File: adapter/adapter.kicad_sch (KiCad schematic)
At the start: 13 parts, among them J1 Serial, J10 Ribbon, J3 Battery charge, J4 RGB, J9 Ribbon, SW1 SW_SPST, SW3 SW_SPDT, U1 Dual MCU: RP2040 + nice!nano

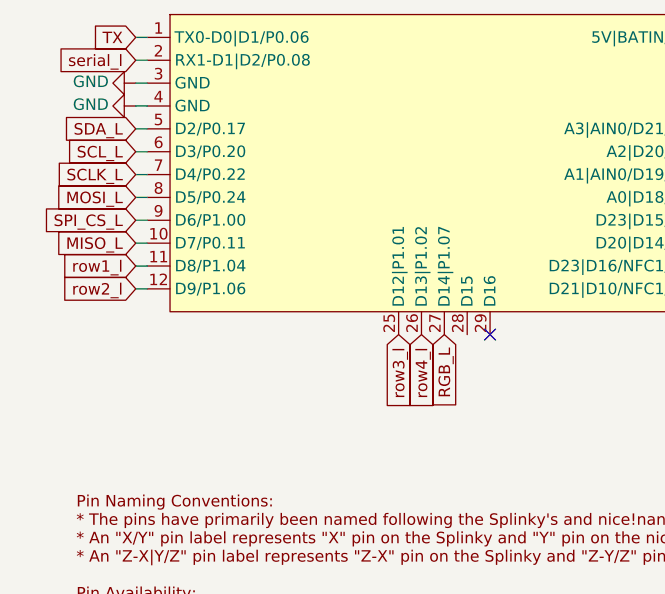
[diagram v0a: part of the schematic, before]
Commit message: sch: properly assign spi pins
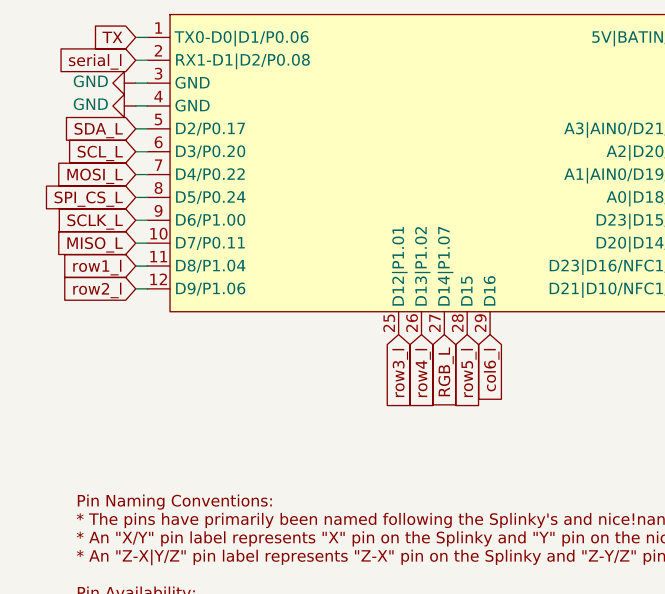
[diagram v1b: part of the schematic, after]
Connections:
- net MOSI_L: now also U1.7 (D4/P0.22); no longer U1.8 (D5/P0.24)
- net SCLK_L: now also U1.9 (D6/P1.00); no longer U1.7 (D4/P0.22)
- net SPI_CS_L: now also U1.8 (D5/P0.24); no longer U1.9 (D6/P1.00)
- net col6_l: now also U1.29 (D16)
- net row5_l: now also U1.28 (D15)
- no-connect marks 3 -> 2

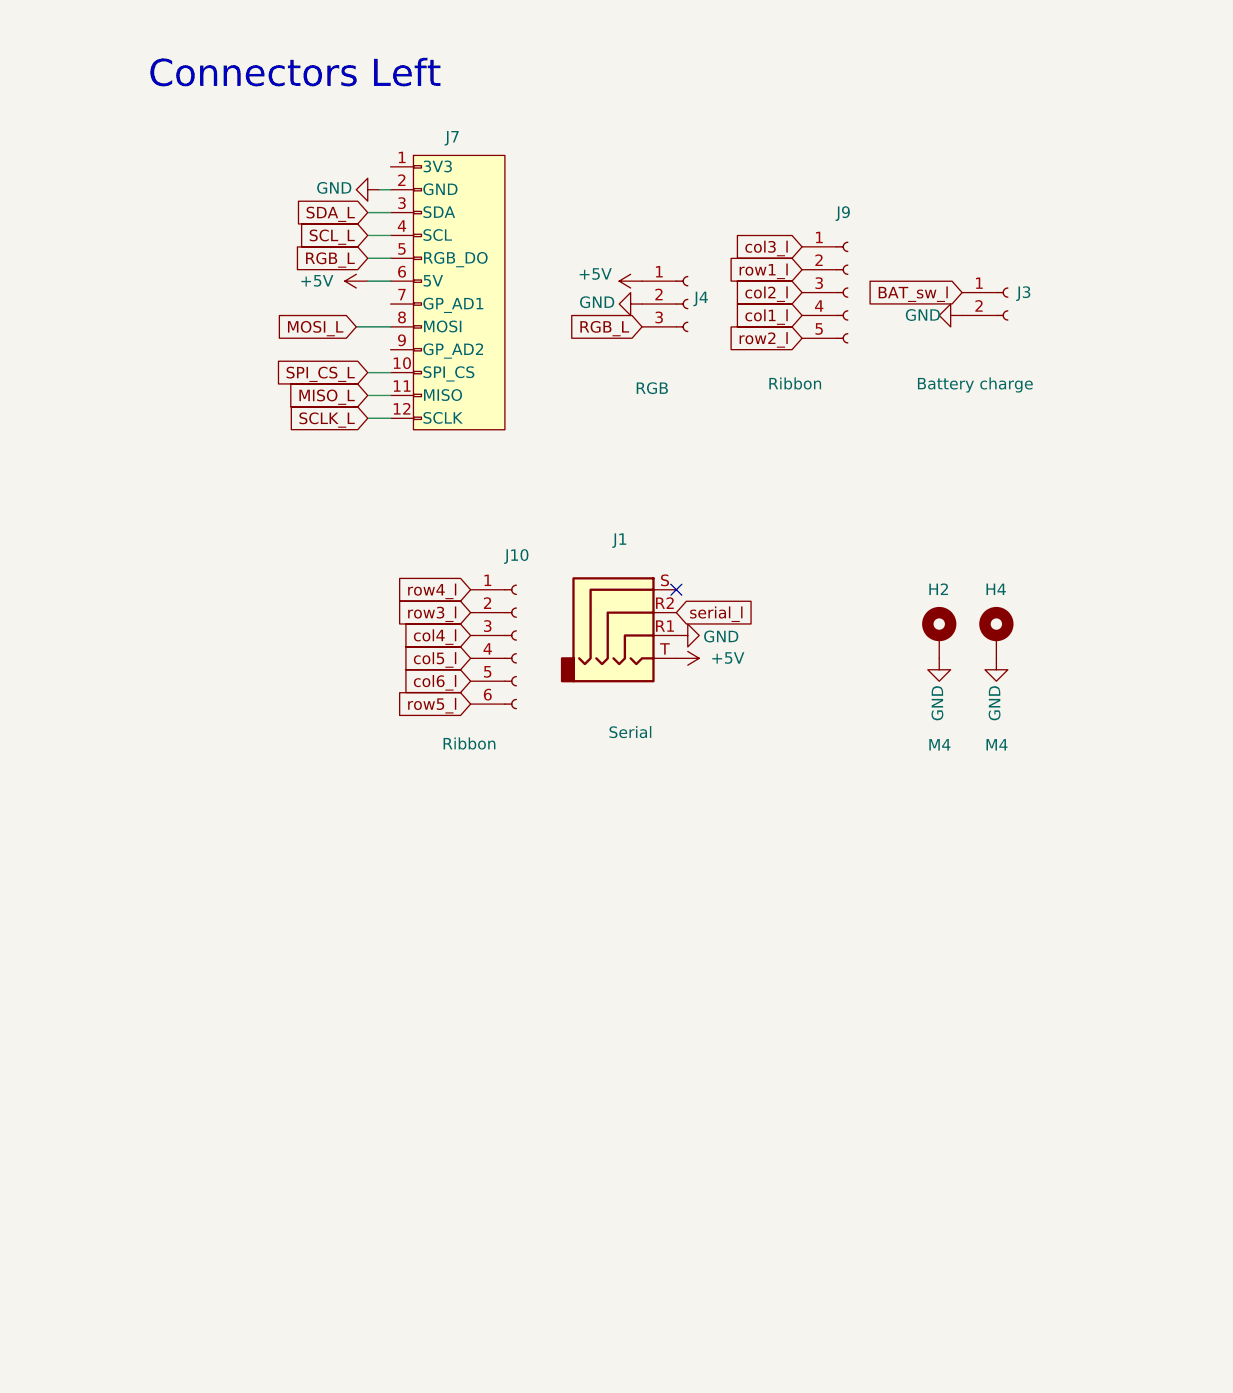
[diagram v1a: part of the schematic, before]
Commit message: sch: add vik connector with jumper to cut for cirque
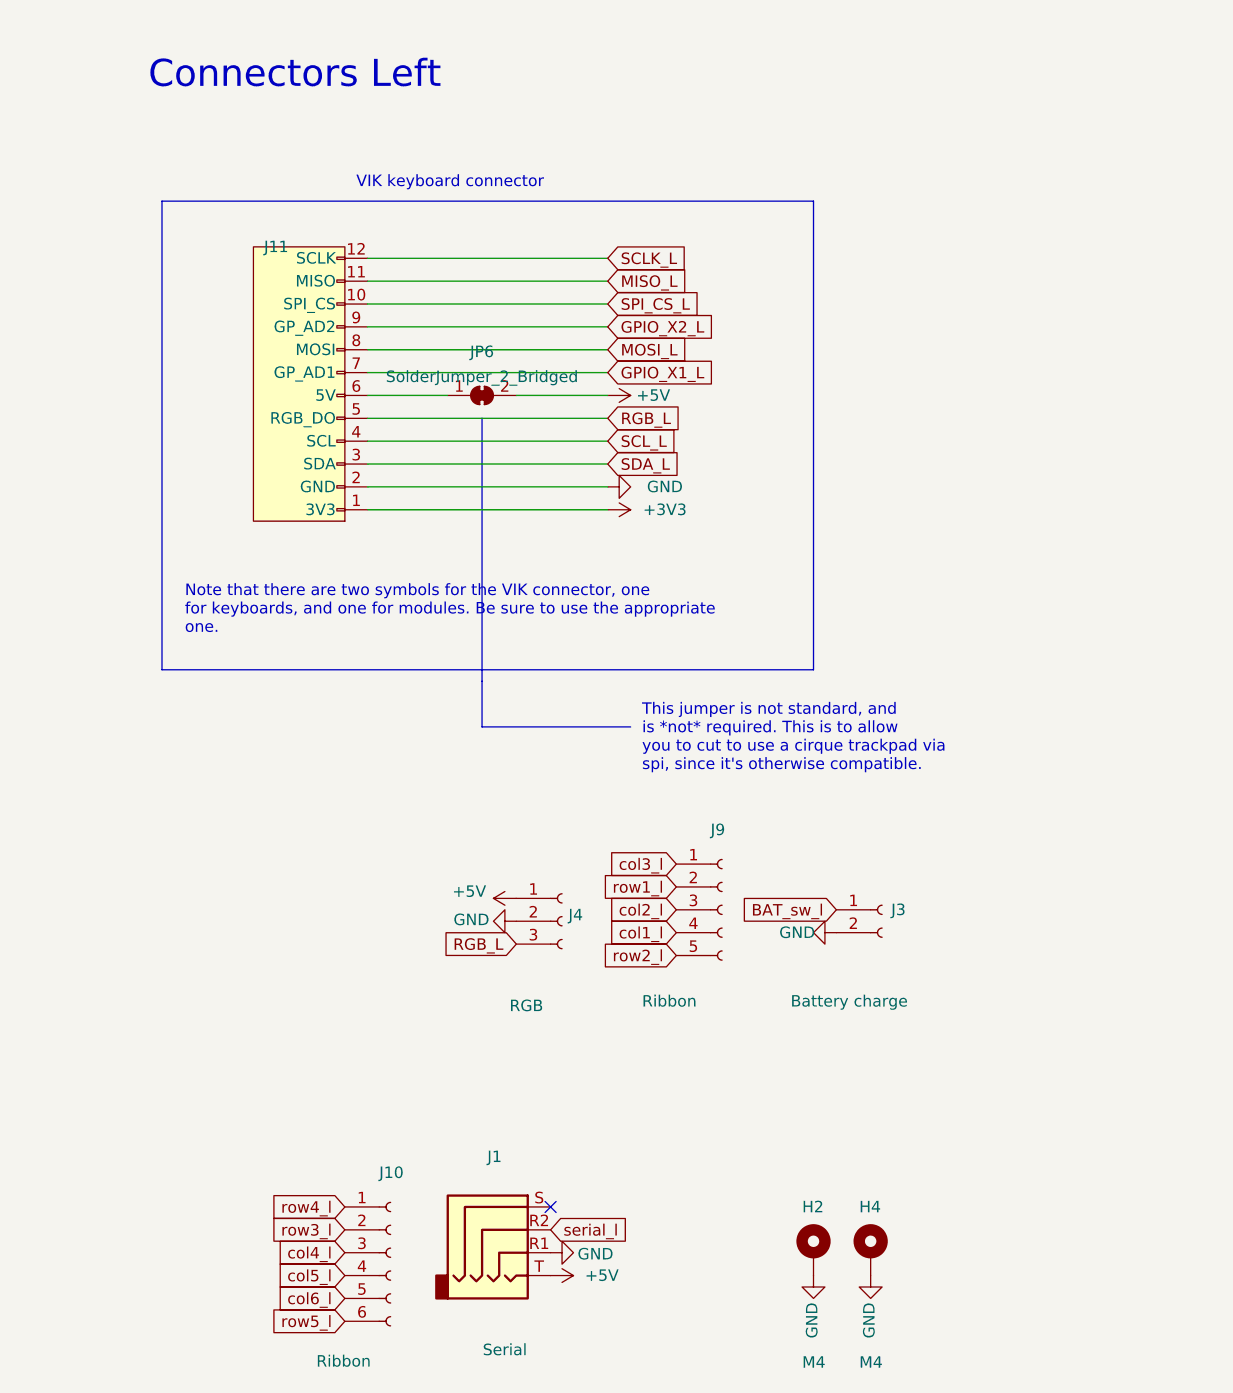
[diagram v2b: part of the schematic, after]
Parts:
- removed J7: ~, vik:vik-keyboard-connector-horizontal, symbol vik:vik-keyboard-connector
- added J11: ~, vik:vik-keyboard-connector-horizontal, symbol vik:vik-keyboard-connector
- added JP6: SolderJumper_2_Bridged, Jumper:SolderJumper-2_P1.3mm_Bridged_Pad1.0x1.5mm, symbol Jumper:SolderJumper_2_Bridged
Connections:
- net +3V3: now also J11.1 (3V3)
- net +5V: now also JP6.2 (B)
- net GND: now also J11.2 (GND)
- net MISO_L: now also J11.11 (MISO)
- net MOSI_L: now also J11.8 (MOSI)
- net RGB_L: now also J11.5 (RGB_DO)
- net SCLK_L: now also J11.12 (SCLK)
- net SCL_L: now also J11.4 (SCL)
- net SDA_L: now also J11.3 (SDA)
- net SPI_CS_L: now also J11.10 (SPI_CS)
- new net: J11.6 (5V), JP6.1 (A)
- new net GPIO_X1_L: J11.7 (GP_AD1)
- new net GPIO_X2_L: J11.9 (GP_AD2)
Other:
- note added: "Note that there are two symbols for the VIK connector, one for keyboards, and one for modules. Be sure to use the appropriate one."
- note added: "This jumper is not standard, and is *not* required. This is to allow you to cut to use a cirque trackpad via spi, since it's otherwise compatible."
- note added: "VIK keyboard connector"
- moved on the sheet: H2, H4, J1, J10, J3, J4, J9

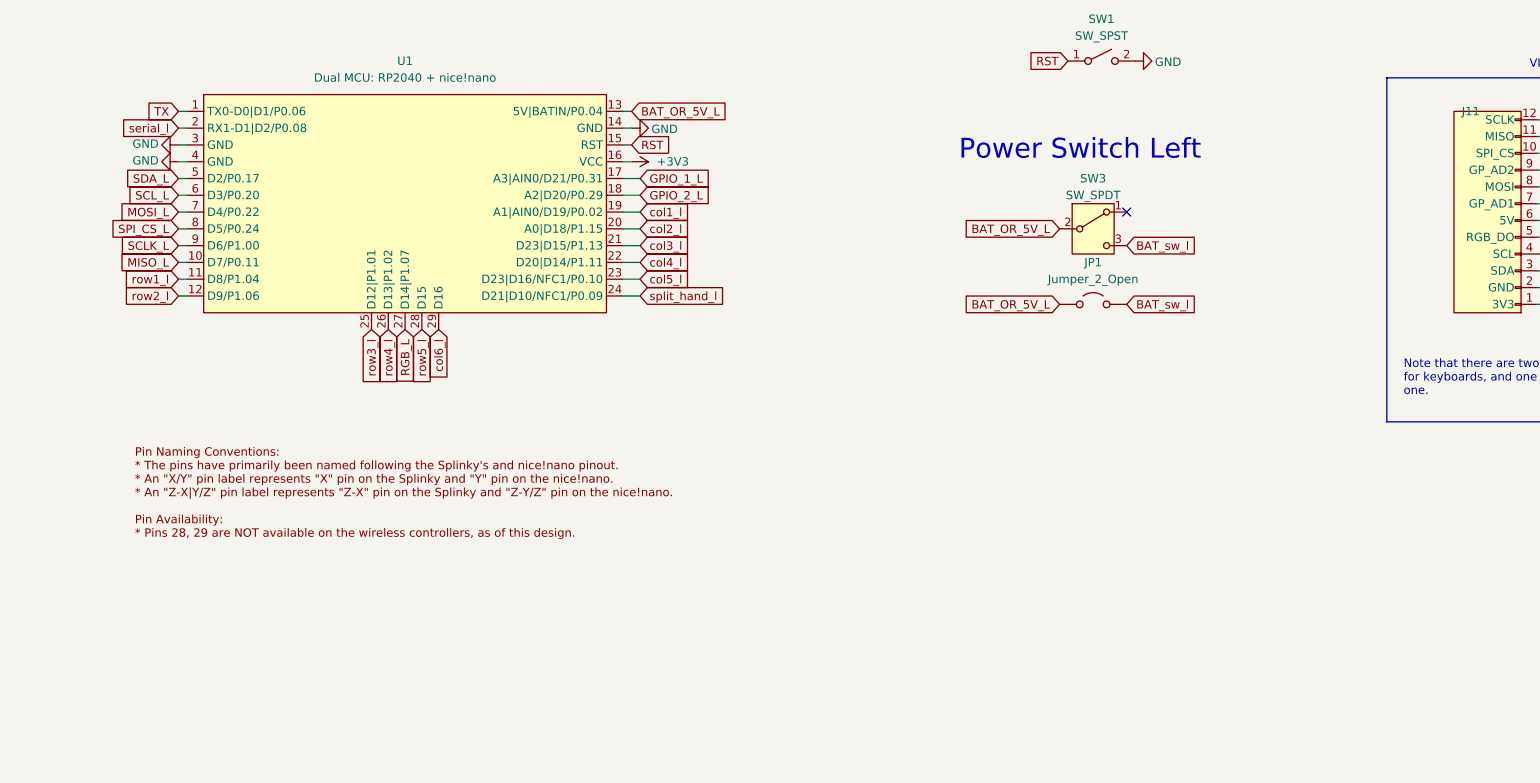
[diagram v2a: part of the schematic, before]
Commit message: sch: add jumpers for handling 5v
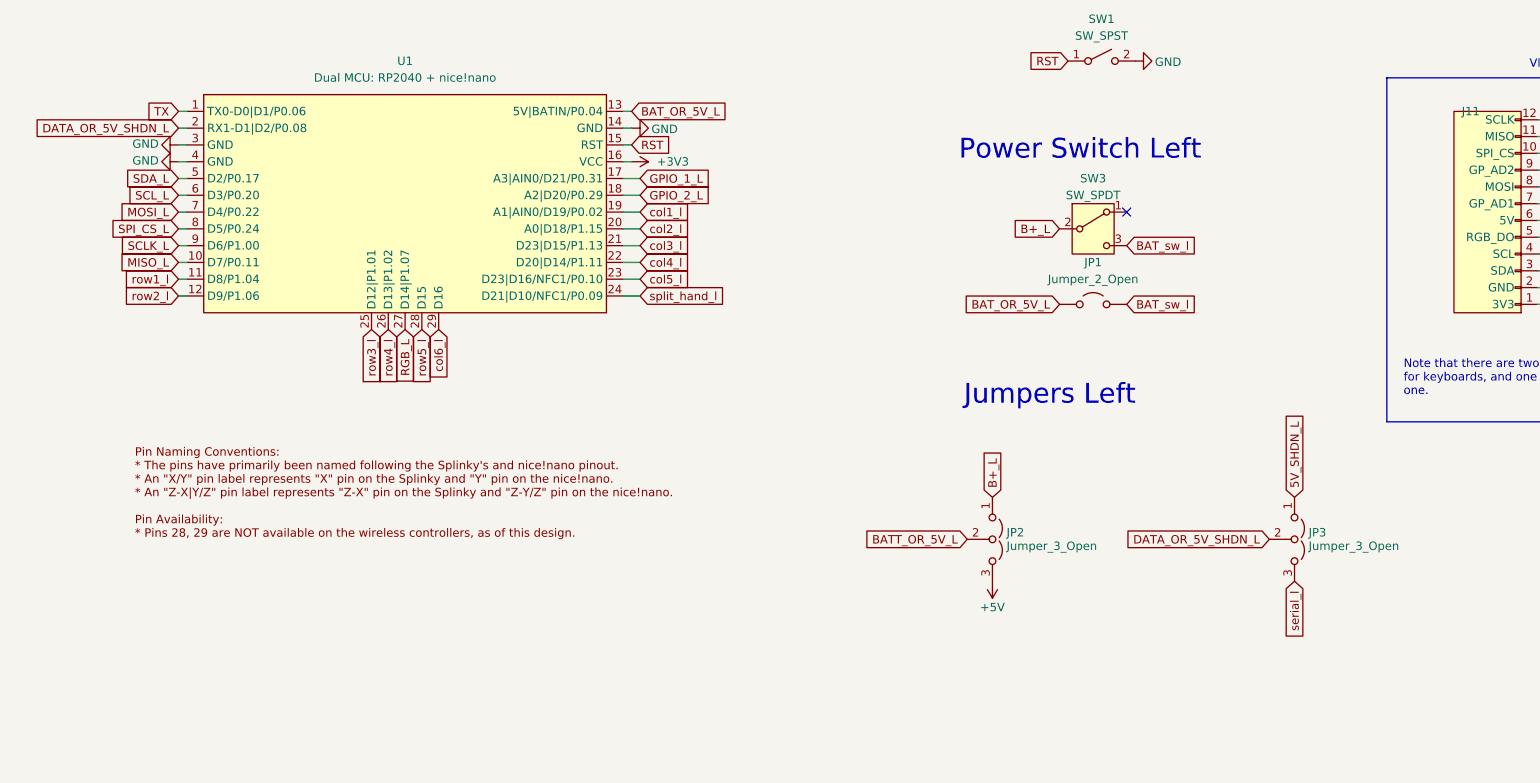
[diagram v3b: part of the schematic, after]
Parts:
- added JP2, JP3: Jumper_3_Open, Jumper:SolderJumper-3_P1.3mm_Open_RoundedPad1.0x1.5mm, symbol Jumper:Jumper_3_Open
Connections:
- net +5V: now also JP2.3 (B)
- net BAT_OR_5V_L: no longer SW3.2 (B)
- net serial_l: now also JP3.3 (B); no longer U1.2 (RX1-D1|D2/P0.08)
- new net 5V_SHDN_L: JP3.1 (A)
- new net B+_L: JP2.1 (A), SW3.2 (B)
- new net BATT_OR_5V_L: JP2.2 (C)
- new net DATA_OR_5V_SHDN_L: JP3.2 (C), U1.2 (RX1-D1|D2/P0.08)
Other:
- note added: "Jumpers Left"

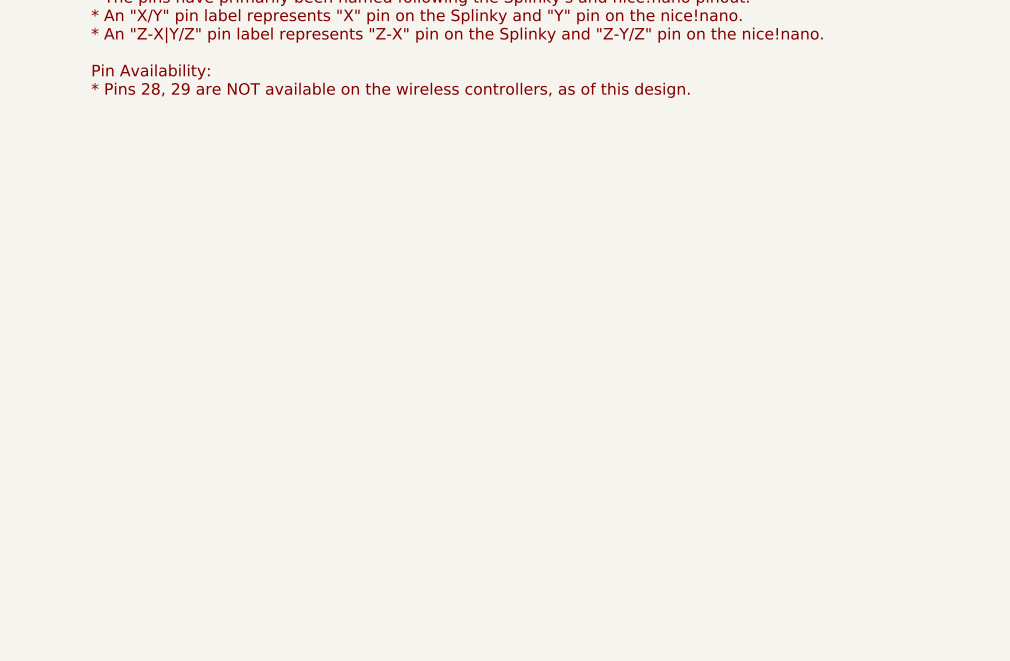
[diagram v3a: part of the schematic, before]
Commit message: sch: add voltage boost circuit
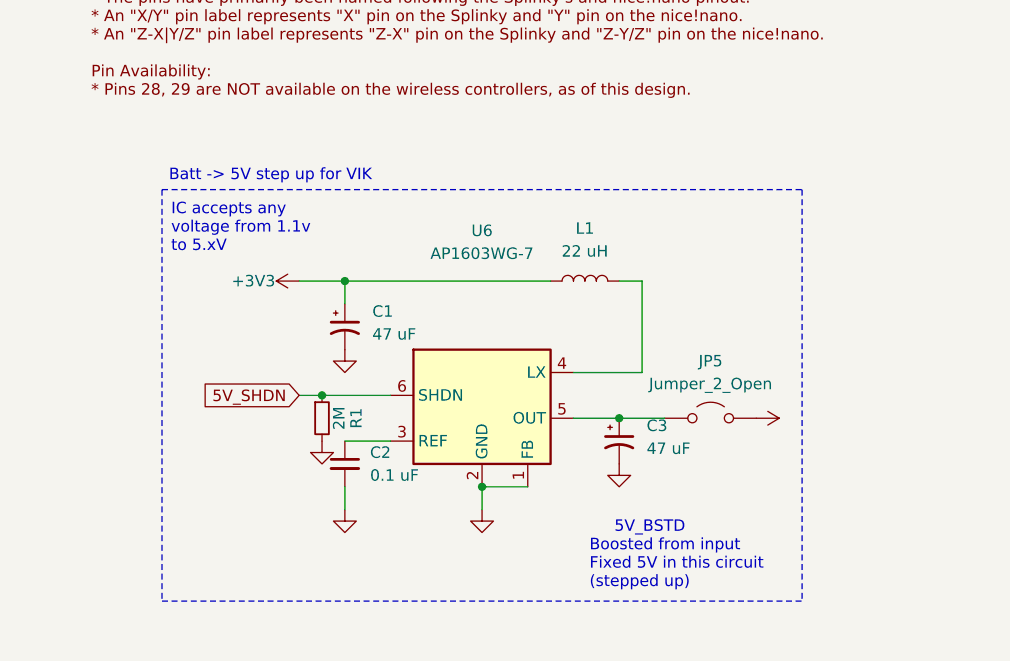
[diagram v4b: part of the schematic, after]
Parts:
- added C1, C3: 47 uF, Capacitor_SMD:C_0603_1608Metric, symbol Device:C_Polarized_Small_US
- added C2: 0.1 uF, Capacitor_SMD:C_0402_1005Metric, symbol Device:C_Small
- added JP5: Jumper_2_Open, Jumper:SolderJumper-2_P1.3mm_Open_RoundedPad1.0x1.5mm, symbol Jumper:Jumper_2_Open
- added L1: 22 uH, Inductor_SMD:L_0603_1608Metric, symbol Device:L
- added R1: 2M, Resistor_SMD:R_0402_1005Metric_Pad0.72x0.64mm_HandSolder, symbol Device:R_Small
- added U6: AP1603WG-7, Package_TO_SOT_SMD:SOT-23-6, symbol AP1603WG-7:AP1603WG-7
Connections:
- net +3V3: now also C1.1, L1.1
- net +5V: now also JP5.2 (B)
- net GND: now also C1.2, C2.2, C3.2, R1.2, U6.1 (FB), U6.2 (GND)
- new net: L1.2, U6.4 (LX)
- new net: C2.1, U6.3 (REF)
- new net: C3.1, JP5.1 (A), U6.5 (OUT)
- new net 5V_SHDN: R1.1, U6.6 (SHDN)
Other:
- note added: "5V_BSTD Boosted from input Fixed 5V in this circuit (stepped up)"
- note added: "Batt -> 5V step up for VIK"
- note added: "IC accepts any voltage from 1.1v to 5.xV"
